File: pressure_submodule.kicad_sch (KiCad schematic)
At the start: 17 parts, among them IC9 PINA350ABSIDDFR, J11 Conn_01x04, Q9 BSZ0902NSATMA1

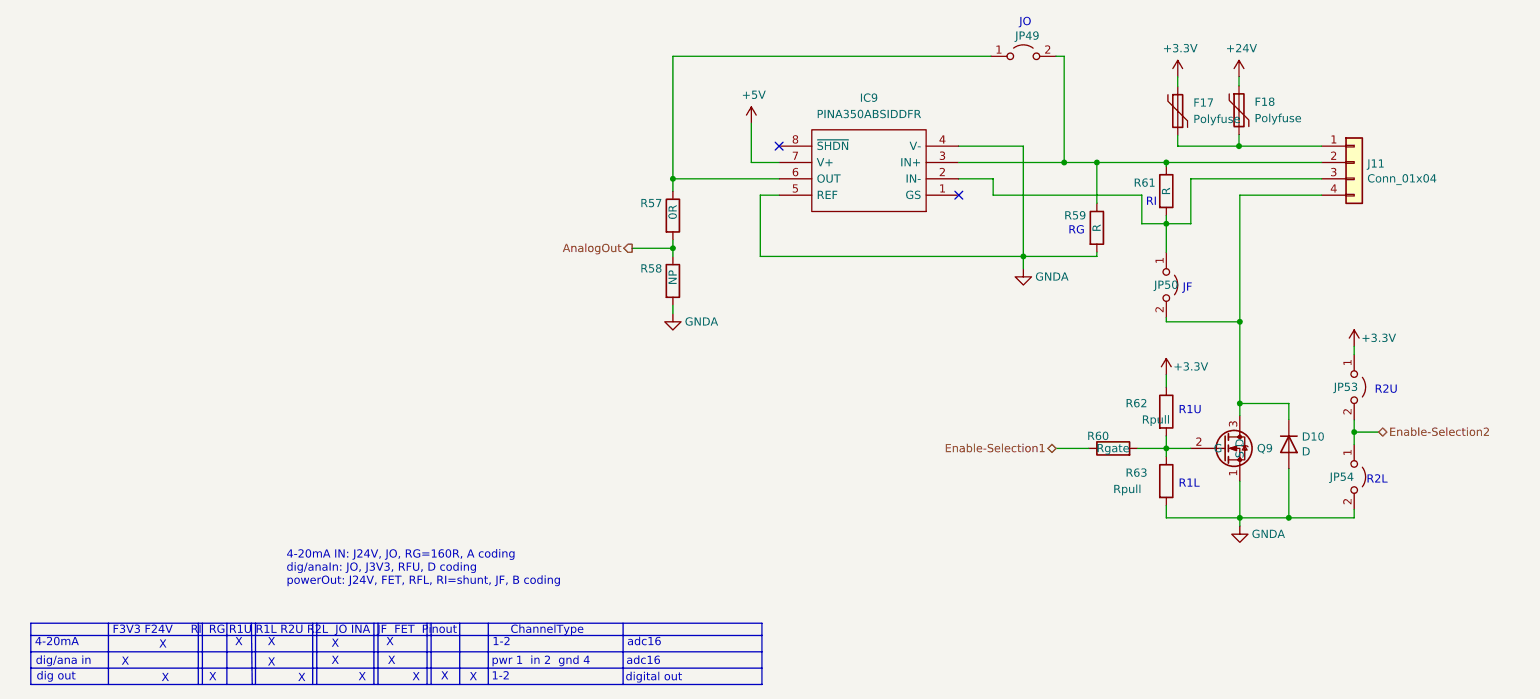
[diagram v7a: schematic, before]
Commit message: All GNDD and GNDA changed to GND
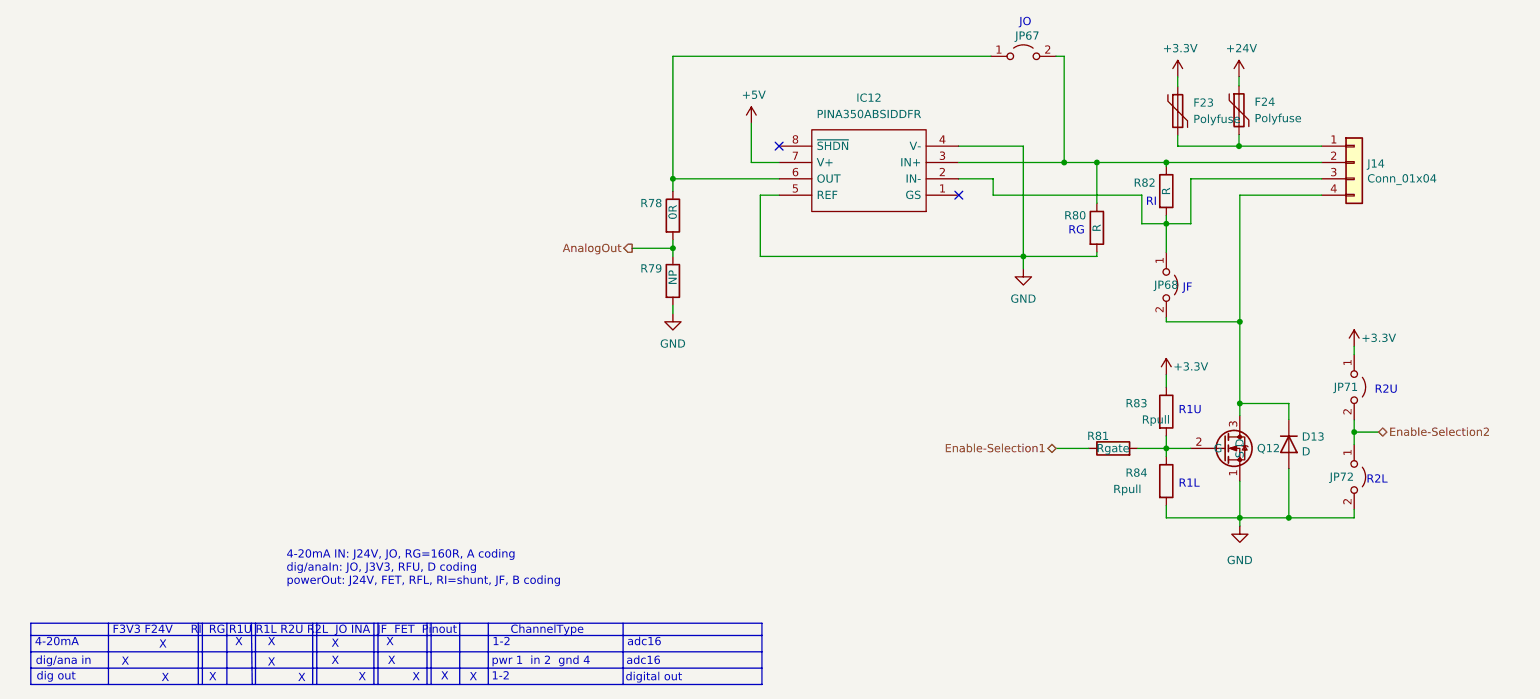
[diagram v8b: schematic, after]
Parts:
- renumbered D10 to D13, F17 to F23, F18 to F24, IC9 to IC12, J11 to J14, JP49 to JP67, JP50 to JP68, JP53 to JP71, JP54 to JP72, Q9 to Q12, R57 to R78, R58 to R79, R59 to R80, R60 to R81, R61 to R82, R62 to R83, R63 to R84
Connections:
- net GNDA renamed GND
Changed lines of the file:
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@@
   (symbol (lib_id "Connector_Generic:Conn_01x04") (at 241.3 89.281 0)
     (in_bom yes) (on_board yes)
-    (property "Reference" "J11" (id 0) (at 243.332 89.4842 0)
+    (property "Reference" "J14" (id 0) (at 243.332 89.4842 0)
       (effects (font (size 1.27 1.27)) (justify left))
     )
@@
   (symbol (lib_id "Jumper:Jumper_2_Open") (at 241.3 124.206 270)
     (in_bom yes) (on_board yes)
-    (property "Reference" "JP53" (id 0) (at 238.125 124.206 90)
+    (property "Reference" "JP71" (id 0) (at 238.125 124.206 90)
       (effects (font (size 1.27 1.27)) (justify left))
     )
@@
   (symbol (lib_id "Jumper:Jumper_2_Open") (at 241.3 138.176 270)
     (in_bom yes) (on_board yes)
-    (property "Reference" "JP54" (id 0) (at 237.49 138.176 90)
+    (property "Reference" "JP72" (id 0) (at 237.49 138.176 90)
       (effects (font (size 1.27 1.27)) (justify left))
     )
@@
     (pin "1")
   )
+  (symbol (lib_id "power:GND") (at 189.865 105.791 0)
+    (in_bom yes) (on_board yes) (fields_autoplaced)
+    (property "Reference" "#PWR0103" (id 0) (at 189.865 112.141 0)
+      (effects (font (size 1.27 1.27)) hide)
+    )
+    (property "Value" "GND" (id 1) (at 189.865 110.49 0))
+    (property "Footprint" "" (id 2) (at 189.865 105.791 0)
+      (effects (font (size 1.27 1.27)) hide)
+    )
+    (property "Datasheet" "" (id 3) (at 189.865 105.791 0)
+      (effects (font (size 1.27 1.27)) hide)
+    )
+    (pin "1")
+  )
   (symbol (lib_id "Device:Polyfuse") (at 223.393 81.153 0)
     (in_bom yes) (on_board yes) (fields_autoplaced)
-    (property "Reference" "F18" (id 0) (at 225.806 79.8829 0)
+    (property "Reference" "F24" (id 0) (at 225.806 79.8829 0)
       (effects (font (size 1.27 1.27)) (justify left))
     )
@@
   (symbol (lib_id "Device:R") (at 212.09 138.811 0)
     (in_bom yes) (on_board yes)
-    (property "Reference" "R63" (id 0) (at 205.74 137.541 0)
+    (property "Reference" "R84" (id 0) (at 205.74 137.541 0)
       (effects (font (size 1.27 1.27)) (justify left))
     )
@@
   (symbol (lib_id "Device:Polyfuse") (at 213.868 81.28 0)
     (in_bom yes) (on_board yes) (fields_autoplaced)
-    (property "Reference" "F17" (id 0) (at 216.281 80.0099 0)
+    (property "Reference" "F23" (id 0) (at 216.281 80.0099 0)
       (effects (font (size 1.27 1.27)) (justify left))
     )
@@
     (pin "2")
   )
-  (symbol (lib_id "power:GNDA") (at 223.52 145.796 0)
-    (in_bom yes) (on_board yes)
-    (property "Reference" "#PWR0107" (id 0) (at 223.52 152.146 0)
-      (effects (font (size 1.27 1.27)) hide)
-    )
-    (property "Value" "GNDA" (id 1) (at 227.965 147.066 0))
-    (property "Footprint" "" (id 2) (at 223.52 145.796 0)
-      (effects (font (size 1.27 1.27)) hide)
-    )
-    (property "Datasheet" "" (id 3) (at 223.52 145.796 0)
-      (effects (font (size 1.27 1.27)) hide)
-    )
-    (pin "1")
-  )
   (symbol (lib_id "Jumper:Jumper_2_Open") (at 189.865 72.771 0)
     (in_bom yes) (on_board yes)
-    (property "Reference" "JP49" (id 0) (at 188.595 69.596 0)
+    (property "Reference" "JP67" (id 0) (at 188.595 69.596 0)
       (effects (font (size 1.27 1.27)) (justify left))
     )
@@
   (symbol (lib_id "Jumper:Jumper_2_Open") (at 212.09 108.331 270)
     (in_bom yes) (on_board yes)
-    (property "Reference" "JP50" (id 0) (at 210.185 108.331 90)
+    (property "Reference" "JP68" (id 0) (at 210.185 108.331 90)
       (effects (font (size 1.27 1.27)) (justify left))
     )
@@
   (symbol (lib_id "Device:R") (at 135.382 97.536 0)
     (in_bom yes) (on_board yes)
-    (property "Reference" "R57" (id 0) (at 130.302 95.631 0)
+    (property "Reference" "R78" (id 0) (at 130.302 95.631 0)
       (effects (font (size 1.27 1.27)) (justify left))
     )
@@
   (symbol (lib_id "PINA350ABSIDDFR:PINA350ABSIDDFR") (at 179.832 94.361 180)
     (in_bom yes) (on_board yes) (fields_autoplaced)
-    (property "Reference" "IC9" (id 0) (at 165.862 79.248 0))
+    (property "Reference" "IC12" (id 0) (at 165.862 79.248 0))
     (property "Value" "PINA350ABSIDDFR" (id 1) (at 165.862 81.788 0))
     (property "Footprint" "SOT65P280X110-8N" (id 2) (at 155.702 96.901 0)
@@
   (symbol (lib_id "Device:R") (at 201.295 99.441 0)
     (in_bom yes) (on_board yes)
-    (property "Reference" "R59" (id 0) (at 196.215 97.536 0)
+    (property "Reference" "R80" (id 0) (at 196.215 97.536 0)
       (effects (font (size 1.27 1.27)) (justify left))
     )
@@
   (symbol (lib_id "Device:R") (at 135.382 107.696 0)
     (in_bom yes) (on_board yes)
-    (property "Reference" "R58" (id 0) (at 130.302 105.791 0)
+    (property "Reference" "R79" (id 0) (at 130.302 105.791 0)
       (effects (font (size 1.27 1.27)) (justify left))
     )
@@
   (symbol (lib_id "Device:R") (at 212.09 128.016 0)
     (in_bom yes) (on_board yes)
-    (property "Reference" "R62" (id 0) (at 205.74 126.746 0)
+    (property "Reference" "R83" (id 0) (at 205.74 126.746 0)
       (effects (font (size 1.27 1.27)) (justify left))
     )
@@
   (symbol (lib_id "Device:D") (at 231.14 133.096 270)
     (in_bom yes) (on_board yes)
-    (property "Reference" "D10" (id 0) (at 233.1466 131.9276 90)
+    (property "Reference" "D13" (id 0) (at 233.1466 131.9276 90)
       (effects (font (size 1.27 1.27)) (justify left))
     )
@@
     (pin "1")
   )
-  (symbol (lib_id "power:GNDA") (at 135.382 112.776 0)
-    (in_bom yes) (on_board yes)
+  (symbol (lib_id "IOB-rescue:BSZ0902NSATMA1-TXV_Library_Symbols") (at 222.25 133.731 0)
+    (in_bom yes) (on_board yes)
+    (property "Reference" "Q12" (id 0) (at 226.187 133.731 0)
+      (effects (font (size 1.27 1.27)) (justify left))
+    )
+    (property "Value" "BSZ0902NSATMA1" (id 1) (at 226.1616 134.874 0)
+      (effects (font (size 1.27 1.27)) (justify left) hide)
+    )
+    (property "Footprint" "TXV_Library_Footprints:PG_TSDSON-8" (id 2) (at 222.25 133.731 0)
+      (effects (font (size 1.27 1.27)) hide)
+    )
+    (property "Datasheet" "" (id 3) (at 222.25 133.731 0)
+      (effects (font (size 1.27 1.27)) hide)
+    )
+    (pin "1")
+    (pin "2")
+    (pin "3")
+  )
+  (symbol (lib_id "power:GND") (at 223.52 145.796 0)
+    (in_bom yes) (on_board yes) (fields_autoplaced)
+    (property "Reference" "#PWR0107" (id 0) (at 223.52 152.146 0)
+      (effects (font (size 1.27 1.27)) hide)
+    )
+    (property "Value" "GND" (id 1) (at 223.52 151.13 0))
+    (property "Footprint" "" (id 2) (at 223.52 145.796 0)
+      (effects (font (size 1.27 1.27)) hide)
+    )
+    (property "Datasheet" "" (id 3) (at 223.52 145.796 0)
+      (effects (font (size 1.27 1.27)) hide)
+    )
+    (pin "1")
+  )
+  (symbol (lib_id "power:GND") (at 135.382 112.776 0)
+    (in_bom yes) (on_board yes) (fields_autoplaced)
     (property "Reference" "#PWR0101" (id 0) (at 135.382 119.126 0)
       (effects (font (size 1.27 1.27)) hide)
     )
-    (property "Value" "GNDA" (id 1) (at 139.827 114.046 0))
+    (property "Value" "GND" (id 1) (at 135.382 117.475 0))
     (property "Footprint" "" (id 2) (at 135.382 112.776 0)
       (effects (font (size 1.27 1.27)) hide)
@@
     (pin "1")
   )
-  (symbol (lib_id "IOB-rescue:BSZ0902NSATMA1-TXV_Library_Symbols") (at 222.25 133.731 0)
-    (in_bom yes) (on_board yes)
-    (property "Reference" "Q9" (id 0) (at 226.187 133.731 0)
-      (effects (font (size 1.27 1.27)) (justify left))
-    )
-    (property "Value" "BSZ0902NSATMA1" (id 1) (at 226.1616 134.874 0)
-      (effects (font (size 1.27 1.27)) (justify left) hide)
-    )
-    (property "Footprint" "TXV_Library_Footprints:PG_TSDSON-8" (id 2) (at 222.25 133.731 0)
-      (effects (font (size 1.27 1.27)) hide)
-    )
-    (property "Datasheet" "" (id 3) (at 222.25 133.731 0)
-      (effects (font (size 1.27 1.27)) hide)
-    )
-    (pin "1")
-    (pin "2")
-    (pin "3")
-  )
   (symbol (lib_id "Device:R") (at 212.09 93.726 0)
     (in_bom yes) (on_board yes)
-    (property "Reference" "R61" (id 0) (at 207.01 92.456 0)
+    (property "Reference" "R82" (id 0) (at 207.01 92.456 0)
       (effects (font (size 1.27 1.27)) (justify left))
     )
@@
     (pin "1")
   )
-  (symbol (lib_id "power:GNDA") (at 189.865 105.791 0)
-    (in_bom yes) (on_board yes)
-    (property "Reference" "#PWR0103" (id 0) (at 189.865 112.141 0)
-      (effects (font (size 1.27 1.27)) hide)
-    )
-    (property "Value" "GNDA" (id 1) (at 194.31 107.061 0))
-    (property "Footprint" "" (id 2) (at 189.865 105.791 0)
-      (effects (font (size 1.27 1.27)) hide)
-    )
-    (property "Datasheet" "" (id 3) (at 189.865 105.791 0)
-      (effects (font (size 1.27 1.27)) hide)
-    )
-    (pin "1")
-  )
   (symbol (lib_id "Device:R") (at 203.835 133.731 90)
     (in_bom yes) (on_board yes)
-    (property "Reference" "R60" (id 0) (at 203.2 131.826 90)
-      (effects (font (size 1.27 1.27)) (justify left))
-    )
+    (property "Reference" "R81" (id 0) (at 203.2 131.826 90)
+      (effects (font (size 1.27 1.27)) (justify left))
+    )
